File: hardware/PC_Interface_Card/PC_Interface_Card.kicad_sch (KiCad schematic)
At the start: 74 parts, among them J1 GSB1C41110SSHR, J2 DM3BT-DSF-PEJS, J3 Conn_01x10_Pin, Q1 PMOS, SW1 CherryMX, SW2 CherryMX, SW3 CherryMX, SW4 CherryMX, SW5 CherryMX, SW6 TL1240YQ2JBLK, SW7 TL1240YQ2JBLK, U1 USBLC6-2SC6, U2 TLV1117LV33DCYR, U3 MB85RS4MTYPN-GS-AWEWE1, U4 ESP32-S3-WROOM-1

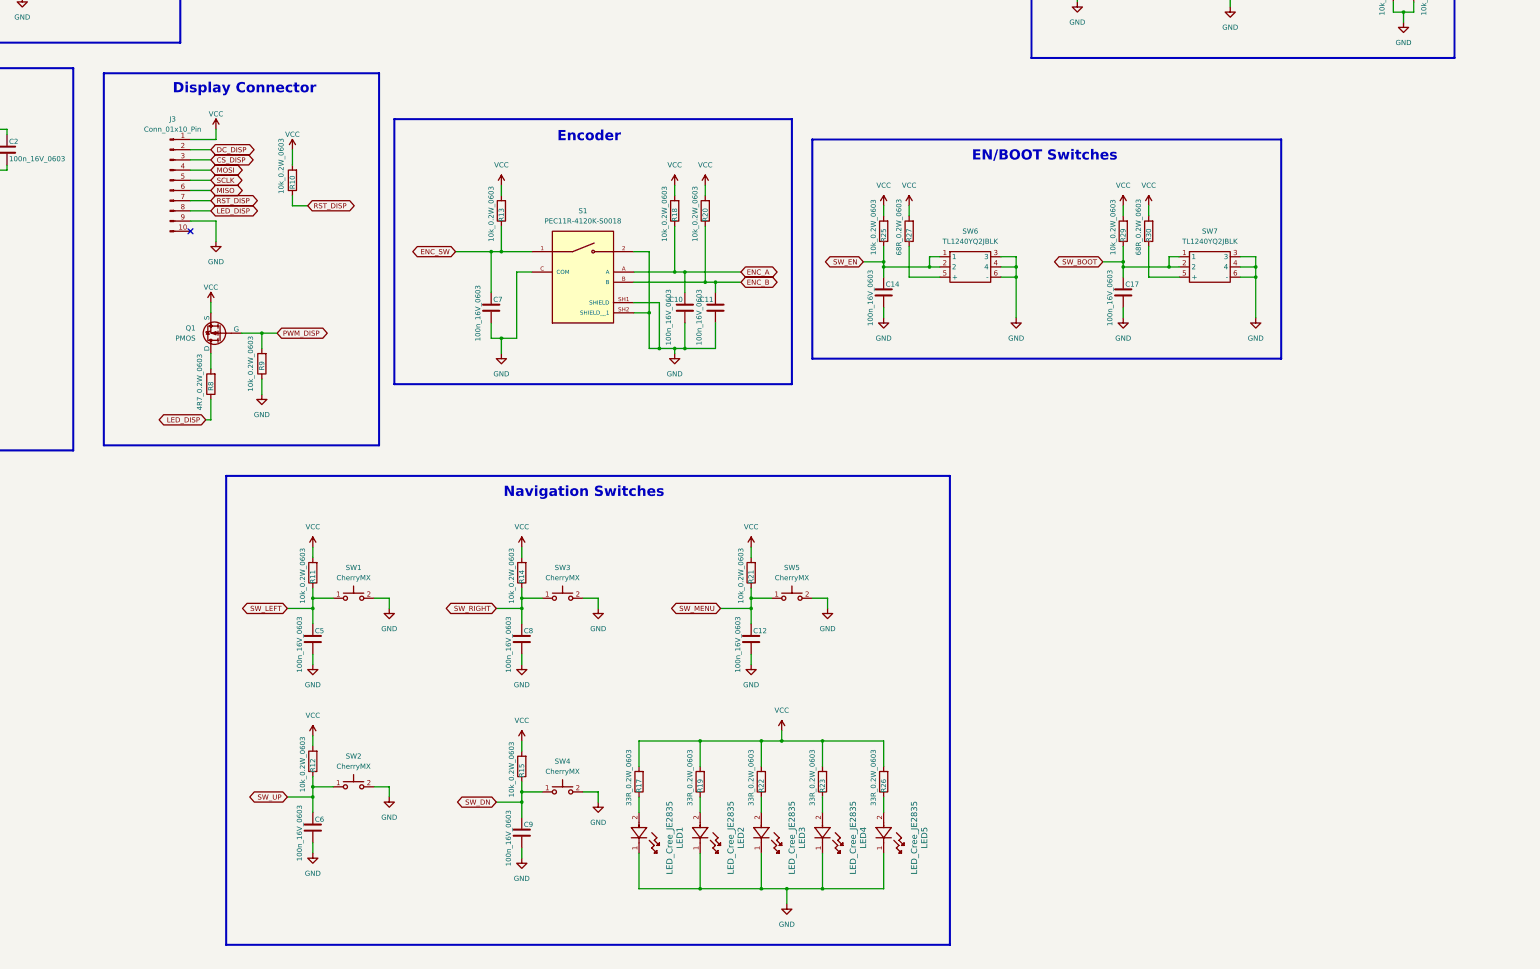
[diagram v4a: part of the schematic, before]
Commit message: More BoM fixes and 3D models, off board parts added.
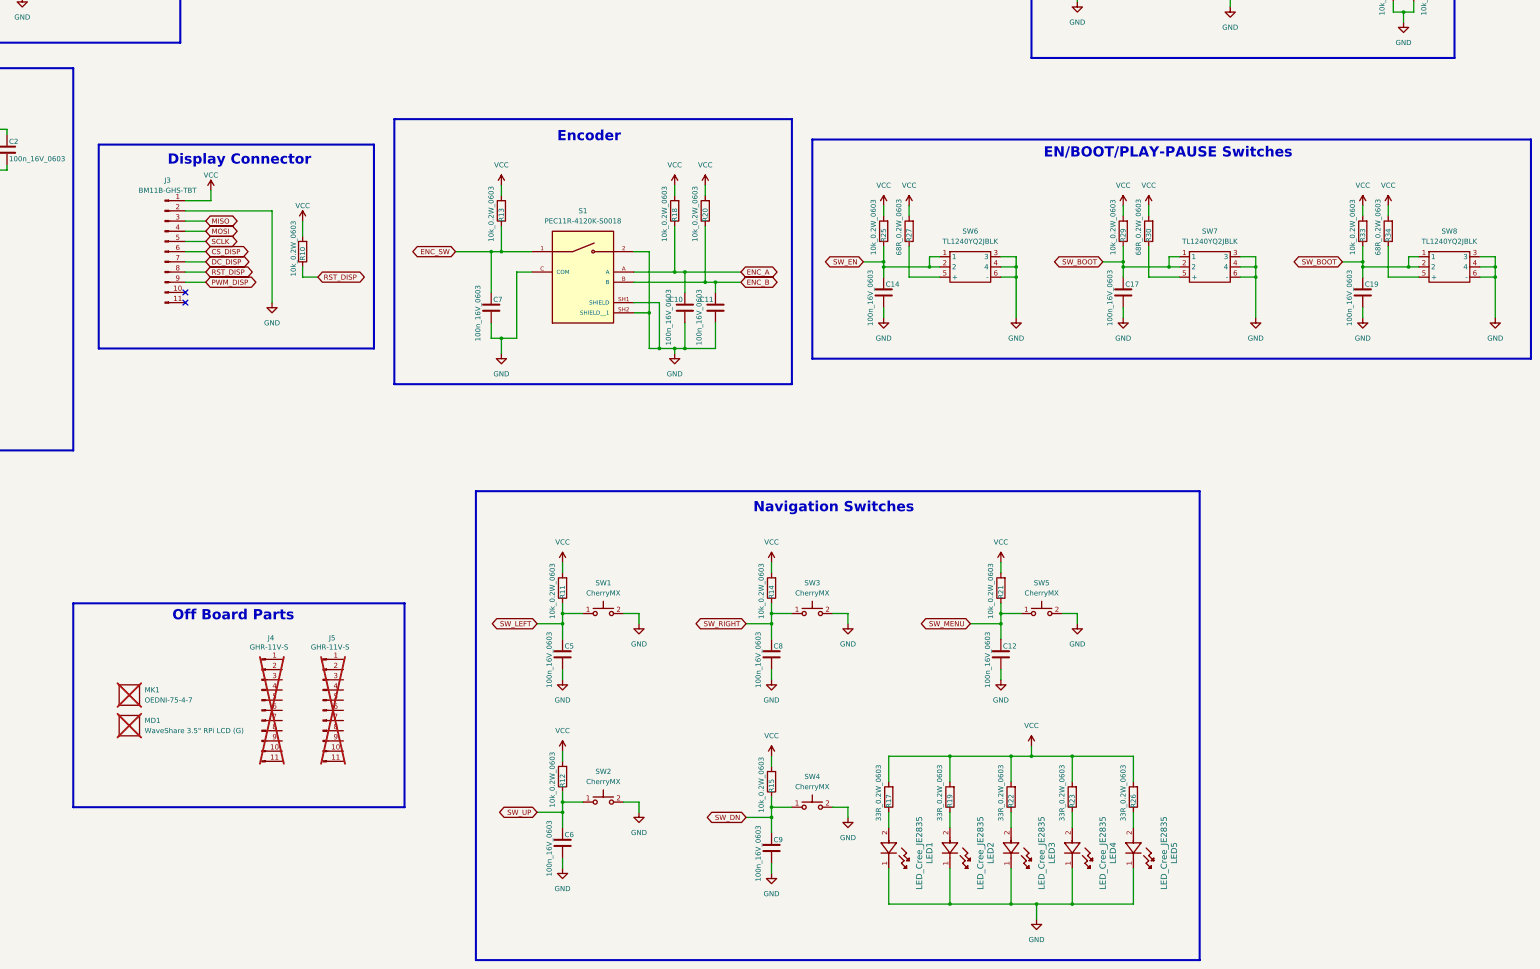
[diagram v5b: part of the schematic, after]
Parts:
- removed Q1: PMOS, Package_TO_SOT_SMD:SOT-23-3, symbol Simulation_SPICE:PMOS
- removed R8: 4R7_0.2W_0603, Resistor_SMD:R_0603_1608Metric, symbol Device:R
- removed R9: 10k_0.2W_0603, Resistor_SMD:R_0603_1608Metric, symbol Device:R
- added C19: 100n_16V_0603, Capacitor_SMD:C_0603_1608Metric, symbol Device:C
- added J4, J5: GHR-11V-S, symbol Connector:Conn_01x11_Pin
- added MD1: WaveShare 3.5" RPi LCD (G), symbol Mechanical_Custom:3.5_In_Display
- added MK1: OEDNI-75-4-7, symbol Mechanical_Custom:OEDNI-75-4-7
- added R33: 10k_0.2W_0603, Resistor_SMD:R_0603_1608Metric, symbol Device:R
- added R34: 68R_0.2W_0603, Resistor_SMD:R_0603_1608Metric, symbol Device:R
- added SW8: TL1240YQ2JBLK, Footprint:TL1240YQ, symbol Custom_Switch_LED:TL1240YQ2JBLK
- C1, C10, C11, C12, C13, C14, C15, C16, C17, C18, C2, C3, C4, C5, C6, C7, C8, C9, CR1, F1, FL1, J1, J2, LED1, LED2, LED3, LED4, LED5, R1, R10, R11, R12, R13, R14, R15, R16, R17, R18, R19, R2, R20, R21, R22, R23, R24, R25, R26, R27, R28, R29, R3, R30, R31, R32, R4, R5, R6, R7, S1, SW1, SW2, SW3, SW4, SW5, SW6, SW7, U1, U2, U3, U4: Vendor (none) -> Digikey
- J3: value Conn_01x10_Pin -> BM11B-GHS-TBT; footprint Connector_PinSocket_1.00mm:PinSocket_1x10_P1.00mm_Vertical -> Footprint_Project_PC_Interface:CONN11_BM11B-GHS-TBTLFSNN_JST; symbol Connector:Conn_01x10_Pin -> Connector:Conn_01x11_Pin; Manufacturer (none) -> JST Sales America Inc.; Manufacturer Part Number (none) -> BM11B-GHS-TBT; Vendor (none) -> Digikey; Vendor Link (none) -> https://www.digikey.in/en/products/detail/jst-sales-america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; Vendor Part Number (none) -> 455-BM11B-GHS-TBTCT-ND
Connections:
- net LED_DISP is gone; now on net RST_DISP: J3.8 (Pin_8)
- net CS_DISP: now also J3.6 (Pin_6); no longer J3.3 (Pin_3)
- net DC_DISP: now also J3.7 (Pin_7); no longer J3.2 (Pin_2)
- net GND: now also J3.2 (Pin_2), C19.2, SW8.3, SW8.4, SW8.6 (-); no longer J3.9 (Pin_9)
- net MISO: now also J3.3 (Pin_3); no longer J3.6 (Pin_6)
- net PWM_DISP: now also J3.9 (Pin_9)
- net RST_DISP: no longer J3.7 (Pin_7)
- net SW_BOOT: now also C19.1, R33.1, SW8.1, SW8.2
- net VCC: now also R33.2, R34.2
- new net: R34.1, SW8.5 (+)
- no-connect marks 15 -> 16
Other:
- note added: "EN/BOOT/PLAY-PAUSE Switches"
- note added: "Off Board Parts"
- note removed: "EN/BOOT Switches"
- moved on the sheet: C12, C5, C6, C8, C9, LED1, LED2, LED3, LED4, LED5, R10, R11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

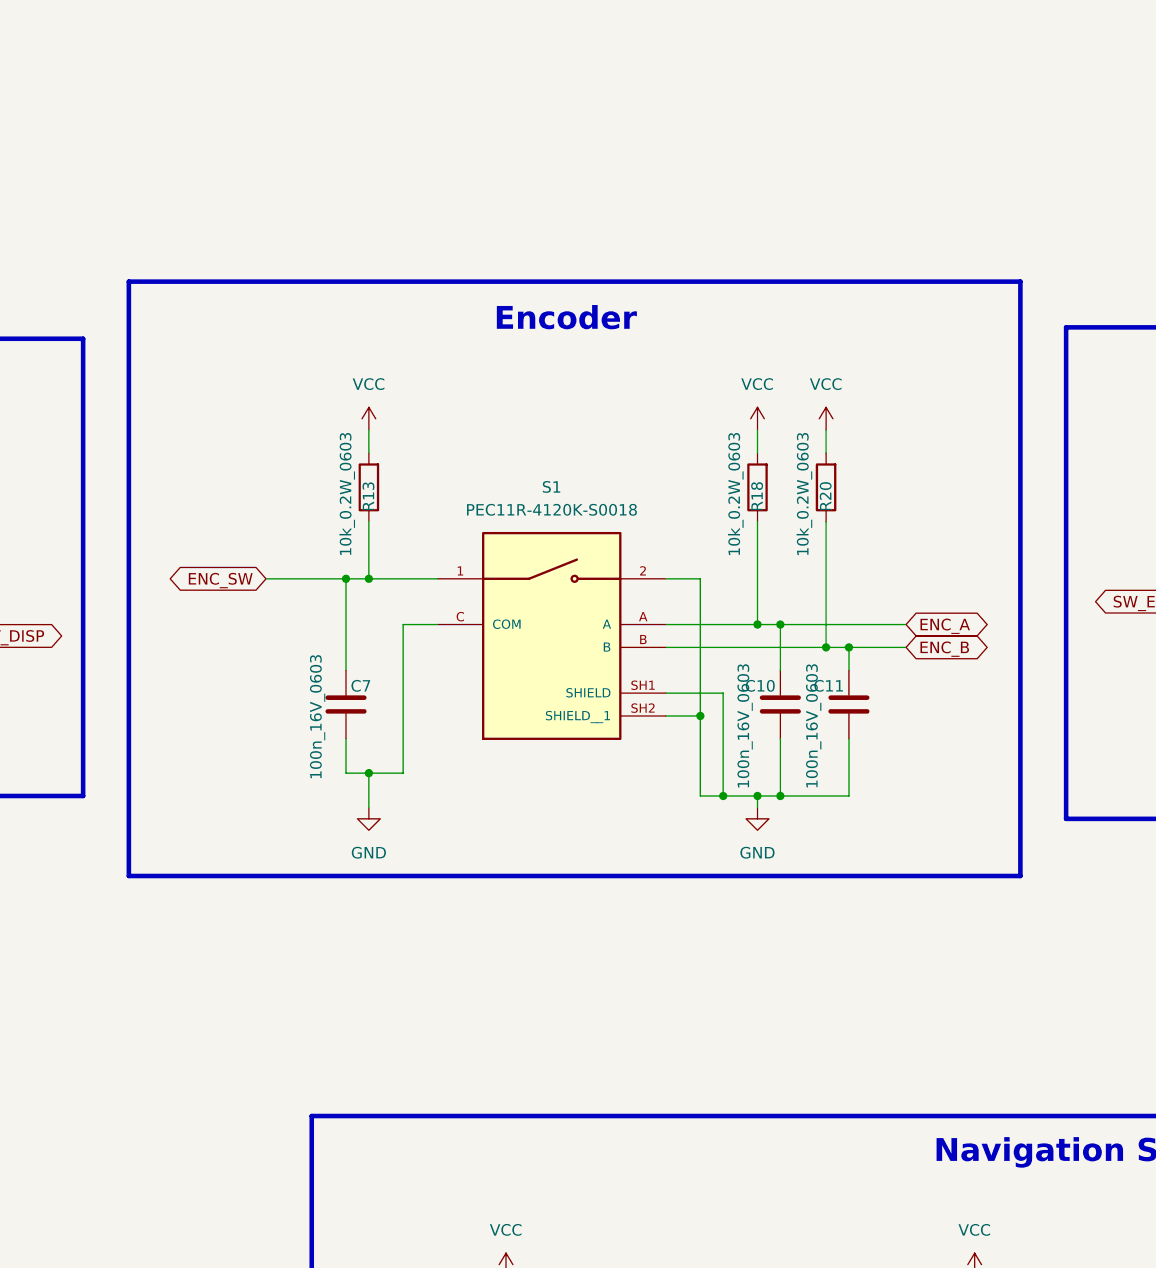
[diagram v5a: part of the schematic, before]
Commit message: Changed encoder to a right angle one
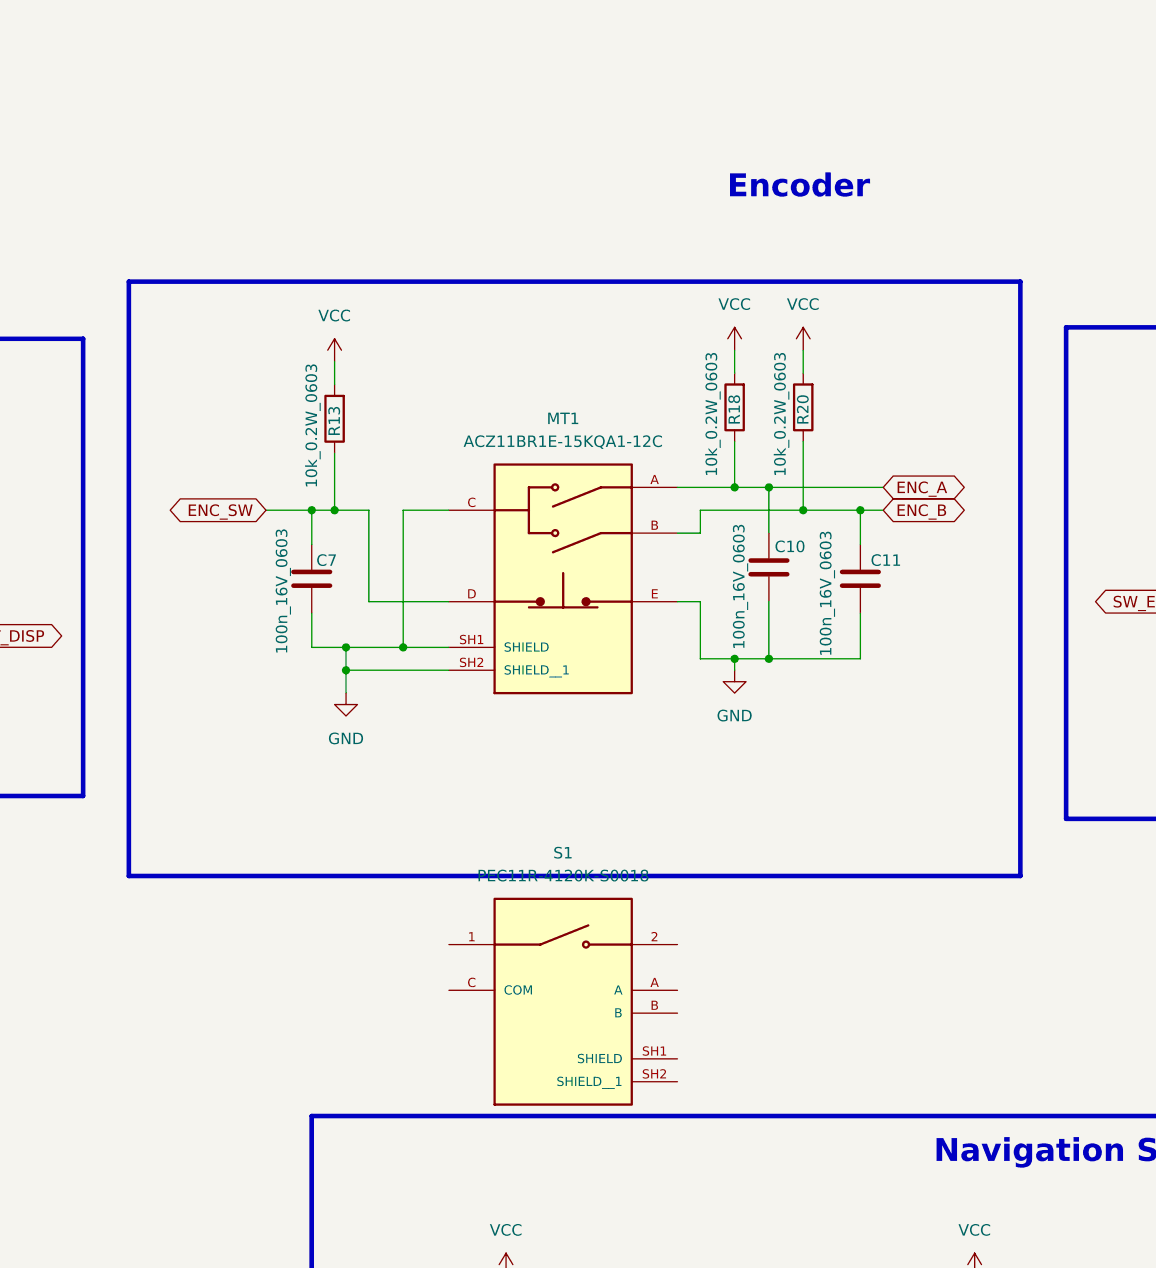
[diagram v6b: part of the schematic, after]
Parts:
- added MT1: ACZ11BR1E-15KQA1-12C, Footprint:XDCR_ACZ11BR1E-15KQA1-12C, symbol ACZ11BR1E-15KQA1-12C:ACZ11BR1E-15KQA1-12C
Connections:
- net ENC_A: now also MT1.A; no longer S1.A
- net ENC_B: now also MT1.B; no longer S1.B
- net ENC_SW: now also MT1.D; no longer S1.1
- net GND: now also MT1.C, MT1.E, MT1.SH1 (SHIELD), MT1.SH2 (SHIELD__1); no longer S1.2, S1.C (COM), S1.SH1 (SHIELD), S1.SH2 (SHIELD__1)
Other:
- moved on the sheet: C10, C11, C7, R13, R18, R20, S1

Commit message: footprint fixes
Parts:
- removed S1: PEC11R-4120K-S0018, Footprint:XDCR_PEC11R-4120K-S0018, symbol PEC11R-4120K-S0018:PEC11R-4120K-S0018
- J3: symbol Connector:Conn_01x11_Pin -> Connector:Conn_01x13_Pin
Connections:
- net GND: now also J3.12 (Pin_12), J3.13 (Pin_13)
- net SW_BOOT: no longer C17.1, R29.1, SW7.1, SW7.2
- net SW_EN: now also C17.1, R29.1, SW7.1, SW7.2
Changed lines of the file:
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@@
 	(rectangle
 		(start 170.18 160.02)
-		(end 238.76 210.82)
+		(end 238.76 213.36)
 		(stroke
 			(width 0.508)
@@
 	)
 	(junction
+		(at 213.36 204.47)
+		(diameter 0)
+		(color 0 0 0 0)
+	)
+	(junction
 		(at 123.19 201.93)
 		(diameter 0)
@@
 	)
 	(junction
+		(at 213.36 201.93)
+		(diameter 0)
+		(color 0 0 0 0)
+	)
+	(junction
 		(at 285.75 326.39)
 		(diameter 0)
@@
 	(wire
 		(pts
+			(xy 191.77 201.93) (xy 213.36 201.93)
+		)
+		(stroke
+			(width 0)
+			(type default)
+		)
+	)
+	(wire
+		(pts
 			(xy 121.92 201.93) (xy 123.19 201.93)
 		)
@@
 	(wire
 		(pts
+			(xy 213.36 204.47) (xy 213.36 205.74)
+		)
+		(stroke
+			(width 0)
+			(type default)
+		)
+	)
+	(wire
+		(pts
 			(xy 369.57 81.28) (xy 374.65 81.28)
 		)
@@
 	(wire
 		(pts
+			(xy 213.36 201.93) (xy 213.36 204.47)
+		)
+		(stroke
+			(width 0)
+			(type default)
+		)
+	)
+	(wire
+		(pts
 			(xy 382.27 312.42) (xy 382.27 318.77)
 		)
@@
 	(wire
 		(pts
-			(xy 213.36 176.53) (xy 213.36 199.39)
+			(xy 213.36 176.53) (xy 213.36 201.93)
 		)
 		(stroke
@@
 	(wire
 		(pts
+			(xy 191.77 204.47) (xy 213.36 204.47)
+		)
+		(stroke
+			(width 0)
+			(type default)
+		)
+	)
+	(wire
+		(pts
 			(xy 279.4 326.39) (xy 285.75 326.39)
 		)
@@
 		)
 	)
+	(global_label "SW_EN"
+		(shape bidirectional)
+		(at 420.37 189.23 180)
+		(fields_autoplaced yes)
+		(effects
+			(font
+				(size 1.27 1.27)
+			)
+			(justify right)
+		)
+		(property "Intersheetrefs" "${INTERSHEET_REFS}"
+			(at 410.1655 189.23 0)
+			(effects
+				(font
+					(size 1.27 1.27)
+				)
+				(justify right)
+				(hide yes)
+			)
+		)
+	)
 	(global_label "MISO"
 		(shape bidirectional)
@@
 		)
 	)
-	(global_label "SW_BOOT"
-		(shape bidirectional)
-		(at 420.37 189.23 180)
-		(fields_autoplaced yes)
-		(effects
-			(font
-				(size 1.27 1.27)
-			)
-			(justify right)
-		)
-		(property "Intersheetrefs" "${INTERSHEET_REFS}"
-			(at 407.7464 189.23 0)
-			(effects
-				(font
-					(size 1.27 1.27)
-				)
-				(justify right)
-				(hide yes)
-			)
-		)
-	)
 	(global_label "CLK_SDMMC"
 		(shape bidirectional)
@@
 	)
 	(symbol
-		(lib_id "PEC11R-4120K-S0018:PEC11R-4120K-S0018")
-		(at 292.1 232.41 0)
-		(unit 1)
-		(exclude_from_sim no)
-		(in_bom yes)
-		(on_board yes)
-		(dnp no)
-		(fields_autoplaced yes)
-		(property "Reference" "S1"
-			(at 292.1 217.17 0)
-			(effects
-				(font
-					(size 1.27 1.27)
-				)
-			)
-		)
-		(property "Value" "PEC11R-4120K-S0018"
-			(at 292.1 219.71 0)
-			(effects
-				(font
-					(size 1.27 1.27)
-				)
-			)
-		)
-		(property "Footprint" "Footprint:XDCR_PEC11R-4120K-S0018"
-			(at 292.1 232.41 0)
-			(effects
-				(font
-					(size 1.27 1.27)
-				)
-				(justify bottom)
-				(hide yes)
-			)
-		)
-		(property "Datasheet" "https://www.bourns.com/docs/Product-Datasheets/PEC11R.pdf"
-			(at 292.1 232.41 0)
-			(effects
-				(font
-					(size 1.27 1.27)
-				)
-				(hide yes)
-			)
-		)
-		(property "Description" "Rotary Encoder Mechanical 18 Quadrature (Incremental) Vertical"
-			(at 292.1 232.41 0)
-			(effects
-				(font
-					(size 1.27 1.27)
-				)
-				(hide yes)
-			)
-		)
-		(property "Manufacturer" "Bourns"
-			(at 292.1 232.41 0)
-			(effects
-				(font
-					(size 1.27 1.27)
-				)
-				(hide yes)
-			)
-		)
-		(property "Vendor" "Digikey"
-			(at 292.1 232.41 0)
-			(effects
-				(font
-					(size 1.27 1.27)
-				)
-				(hide yes)
-			)
-		)
-		(property "Vendor Link" "https://www.digikey.in/en/products/detail/bourns-inc/PEC11R-4120K-S0018/4699211?s=N4IgTCBcDaIAoFEDCBGFAlAtAFhWADANKYDK%2B%2BKAHCALoC%2BQA"
-			(at 292.1 232.41 0)
-			(effects
-				(font
-					(size 1.27 1.27)
-				)
-				(hide yes)
-			)
-		)
-		(property "Vendor Part Number" "PEC11R-4120K-S0018-ND"
-			(at 292.1 232.41 0)
-			(effects
-				(font
-					(size 1.27 1.27)
-				)
-				(hide yes)
-			)
-		)
-		(property "Manufacturer Part Number" "PEC11R-4120K-S0018"
-			(at 292.1 232.41 0)
-			(effects
-				(font
-					(size 1.27 1.27)
-				)
-				(hide yes)
-			)
-		)
-		(property "Sim.Device" ""
-			(at 292.1 232.41 0)
-			(effects
-				(font
-					(size 1.27 1.27)
-				)
-				(hide yes)
-			)
-		)
-		(property "Sim.Pins" ""
-			(at 292.1 232.41 0)
-			(effects
-				(font
-					(size 1.27 1.27)
-				)
-				(hide yes)
-			)
-		)
-		(property "Sim.Type" ""
-			(at 292.1 232.41 0)
-			(effects
-				(font
-					(size 1.27 1.27)
-				)
-				(hide yes)
-			)
-		)
-		(pin "SH1"
-		)
-		(pin "SH2"
-		)
-		(pin "A"
-		)
-		(pin "1"
-		)
-		(pin "2"
-		)
-		(pin "C"
-		)
-		(pin "B"
-		)
-		(instances
-			(project ""
-				(path "/84eb640b-174f-4748-a6d8-0439a1f868d2"
-					(reference "S1")
-					(unit 1)
-				)
-			)
-		)
-	)
-	(symbol
 		(lib_id "power:VCC")
 		(at 425.45 175.26 0)
@@
 	)
 	(symbol
-		(lib_id "Connector:Conn_01x11_Pin")
-		(at 186.69 186.69 0)
+		(lib_id "Connector:Conn_01x13_Pin")
+		(at 186.69 189.23 0)
 		(unit 1)
 		(exclude_from_sim no)
@@
 		)
 		(property "Footprint" "Footprint_Project_PC_Interface:CONN11_BM11B-GHS-TBTLFSNN_JST"
-			(at 186.69 186.69 0)
+			(at 186.69 189.23 0)
 			(effects
 				(font
@@
 		)
 		(property "Datasheet" "~"
-			(at 186.69 186.69 0)
+			(at 186.69 189.23 0)
 			(effects
 				(font
@@
 			)
 		)
-		(property "Description" "Generic connector, single row, 01x11, script generated"
-			(at 186.69 186.69 0)
+		(property "Description" "Generic connector, single row, 01x13, script generated"
+			(at 186.69 189.23 0)
 			(effects
 				(font
@@
 		)
 		(property "Vendor" "Digikey"
-			(at 186.69 186.69 0)
+			(at 186.69 189.23 0)
 			(effects
 				(font
@@
 		)
 		(property "Vendor Link" "https://www.digikey.in/en/products/detail/jst-sales-america-inc/BM11B-GHS-TBT/807809"
-			(at 186.69 186.69 0)
+			(at 186.69 189.23 0)
 			(effects
 				(font
@@
 		)
 		(property "Vendor Part Number" "455-BM11B-GHS-TBTCT-ND"
-			(at 186.69 186.69 0)
+			(at 186.69 189.23 0)
 			(effects
 				(font
@@
 		)
 		(property "Sim.Device" ""
-			(at 186.69 186.69 0)
+			(at 186.69 189.23 0)
 			(effects
 				(font
@@
 		)
 		(property "Sim.Pins" ""
-			(at 186.69 186.69 0)
+			(at 186.69 189.23 0)
 			(effects
 				(font
@@
 		)
 		(property "Sim.Type" ""
-			(at 186.69 186.69 0)
+			(at 186.69 189.23 0)
 			(effects
 				(font
@@
 		)
 		(property "Manufacturer" "JST Sales America Inc."
-			(at 186.69 186.69 0)
+			(at 186.69 189.23 0)
 			(effects
 				(font
@@
 		)
 		(property "Manufacturer Part Number" "BM11B-GHS-TBT"
-			(at 186.69 186.69 0)
+			(at 186.69 189.23 0)
 			(effects
 				(font
@@
 		(pin "11"
 		)
+		(pin "12"
+		)
+		(pin "13"
+		)
 		(instances
 			(project ""
@@
 	(symbol
 		(lib_id "power:GND")
-		(at 213.36 199.39 0)
+		(at 213.36 205.74 0)
 		(unit 1)
 		(exclude_from_sim no)
@@
 		(fields_autoplaced yes)
 		(property "Reference" "#PWR015"
-			(at 213.36 205.74 0)
+			(at 213.36 212.09 0)
 			(effects
 				(font
@@
 		)
 		(property "Value" "GND"
-			(at 213.36 204.47 0)
+			(at 213.36 210.82 0)
 			(effects
 				(font
@@
 		)
 		(property "Footprint" ""
-			(at 213.36 199.39 0)
+			(at 213.36 205.74 0)
 			(effects
 				(font
@@
 		)
 		(property "Datasheet" ""
-			(at 213.36 199.39 0)
+			(at 213.36 205.74 0)
 			(effects
 				(font
@@
 		)
 		(property "Description" "Power symbol creates a global label with name \"GND\" , ground"
-			(at 213.36 199.39 0)
+			(at 213.36 205.74 0)
 			(effects
 				(font
